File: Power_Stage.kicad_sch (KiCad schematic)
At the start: 95 parts, among them CN11 XH-2A, CN12 XH-2A, CN8 XH-2A, CN9 XH-2A, U16 LMR50410XDBVR, U17 LMR50410XDBVR, U3 BQ25792RQMR, U4 INA228AIDGSR, U5 TPS56A37RPAR, U6 IHLP3232DZER3R3M01, U9 SN74LVC1G32DBVR

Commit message: 1
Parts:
- removed C28: 100uF, EasyEDA:CAP-SMD_BD6.3-L6.6-W6.6-LS7.2-R-RD, symbol JLSC:RVT1E101M0607
- removed CN12: XH-2A, EasyEDA:CONN-TH_XH-2A, symbol JLSC:XH-2A
- removed R16: 10K, fb_2, symbol JLSC:0603WAF1002T5E
- removed TP4: 3.3V_AON Test Point, TestPoint:TestPoint_Pad_D1.5mm, symbol Connector:TestPoint
- removed TP5: V_BAT Test Point, TestPoint:TestPoint_Pad_D1.5mm, symbol Connector:TestPoint
- removed TP6: V_BUS Test Point, TestPoint:TestPoint_Pad_D1.5mm, symbol Connector:TestPoint
- added R45: 0603WAF1002T5E, EasyEDA:R0603, symbol JLSC:0603WAF1002T5E
- added R46: 10K, EasyEDA:R0603, symbol JLSC:0603WAF1002T5E
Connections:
- net 5VREG_EN: now also R46.1
- net GND: now also R45.2
- net GNDA: now also R46.2
- net at R23.2, R24.1, U3.16 (TS): now also R45.1

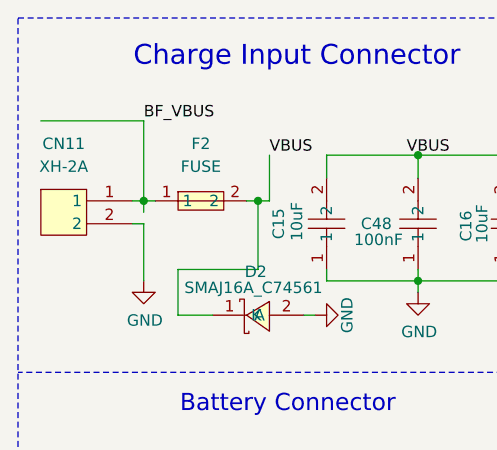
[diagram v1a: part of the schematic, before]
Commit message: micro hdmi eklendi
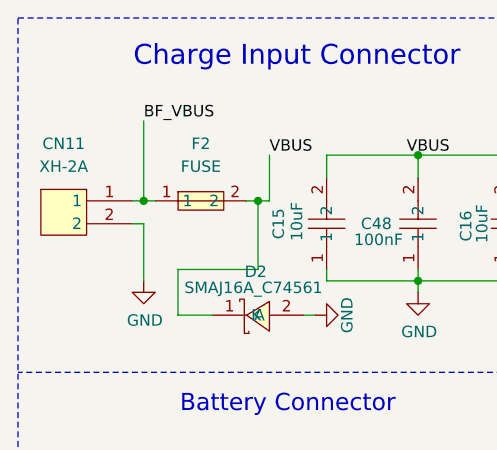
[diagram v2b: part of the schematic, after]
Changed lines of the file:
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@@
 	)
 	(junction
-		(at 35.56 40.64)
-		(diameter 0)
-		(color 0 0 0 0)
-	)
-	(junction
 		(at 82.55 228.6)
 		(diameter 0)
@@
 	)
 	(junction
+		(at 35.56 40.64)
+		(diameter 0)
+		(color 0 0 0 0)
+	)
+	(junction
 		(at 46.99 219.71)
 		(diameter 0)
@@
 	(wire
 		(pts
-			(xy 24.13 31.75) (xy 35.56 31.75)
-		)
-		(stroke
-			(width 0)
-			(type default)
-		)
-	)
-	(wire
-		(pts
 			(xy 287.02 233.68) (xy 287.02 227.33)
 		)
@@
 	(wire
 		(pts
+			(xy 35.56 40.64) (xy 36.83 40.64)
+		)
+		(stroke
+			(width 0)
+			(type default)
+		)
+	)
+	(wire
+		(pts
 			(xy 217.17 160.02) (xy 228.6 160.02)
 		)
@@
 	(wire
 		(pts
-			(xy 35.56 31.75) (xy 35.56 40.64)
-		)
-		(stroke
-			(width 0)
-			(type default)
-		)
-	)
-	(wire
-		(pts
 			(xy 57.15 241.3) (xy 55.88 241.3)
 		)
@@
 	(wire
 		(pts
-			(xy 35.56 40.64) (xy 36.83 40.64)
-		)
-		(stroke
-			(width 0)
-			(type default)
-		)
-	)
-	(wire
-		(pts
 			(xy 69.85 254) (xy 71.12 254)
 		)
@@
 	(wire
 		(pts
-			(xy 35.56 41.91) (xy 35.56 40.64)
-		)
-		(stroke
-			(width 0)
-			(type default)
-		)
-	)
-	(wire
-		(pts
 			(xy 243.84 57.15) (xy 252.73 57.15)
 		)
@@
 		)
 		(stroke
+			(width 0)
+			(type default)
+		)
+	)
+	(wire
+		(pts
+			(xy 35.56 31.75) (xy 35.56 40.64)
+		)
+		(stroke

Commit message: Hdmi
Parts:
- removed D1: SMBJ13A_C188307, EasyEDA:SMB_L4.6-W3.6-LS5.3-RD, symbol JLSC:SMBJ13A_C188307
- added D3: SMBJ14A_C353392, EasyEDA:SMB_L4.4-W3.6-LS5.3-RD, symbol JLSC:SMBJ14A_C353392
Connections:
- net GND: now also D3.2 (A)
- net V_BAT: now also D3.1 (C)
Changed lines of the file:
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@@
 	)
 	(symbol
+		(lib_id "JLSC:SMBJ14A_C353392")
+		(at 71.12 95.25 270)
+		(unit 1)
+		(body_style 1)
+		(exclude_from_sim no)
+		(in_bom yes)
+		(on_board yes)
+		(in_pos_files yes)
+		(dnp no)
+		(property "Reference" "D3"
+			(at 74.93 93.4699 90)
+			(show_name no)
+			(do_not_autoplace no)
+			(effects
+				(font
+					(size 1.27 1.27)
+				)
+				(justify left)
+			)
+		)
+		(property "Value" "SMBJ14A_C353392"
+			(at 50.038 95.504 90)
+			(show_name no)
+			(do_not_autoplace no)
+			(effects
+				(font
+					(size 1.27 1.27)
+				)
+				(justify left)
+			)
+		)
+		(property "Footprint" "EasyEDA:SMB_L4.4-W3.6-LS5.3-RD"
+			(at 63.5 95.25 0)
+			(hide yes)
+			(show_name no)
+			(do_not_autoplace no)
+			(effects
+				(font
+					(size 1.27 1.27)
+				)
+			)
+		)
+		(property "Datasheet" "https://lcsc.com/product-detail/Others_Shandong-Jingdao-Microelectronics-SMBJ14A_C353392.html"
+			(at 60.96 95.25 0)
+			(hide yes)
+			(show_name no)
+			(do_not_autoplace no)
+			(effects
+				(font
+					(size 1.27 1.27)
+				)
+			)
+		)
+		(property "Description" "SMBJ series 600W 14V Uni-directional SMD TVS Diode"
+			(at 71.12 95.25 0)
+			(hide yes)
+			(show_name no)
+			(do_not_autoplace no)
+			(effects
+				(font
+					(size 1.27 1.27)
+				)
+			)
+		)
+		(property "Manufacturer" "晶导微电子"
+			(at 58.42 95.25 0)
+			(hide yes)
+			(show_name no)
+			(do_not_autoplace no)
+			(effects
+				(font
+					(size 1.27 1.27)
+				)
+			)
+		)
+		(property "MPN" "SMBJ14A"
+			(at 55.88 95.25 0)
+			(hide yes)
+			(show_name no)
+			(do_not_autoplace no)
+			(effects
+				(font
+					(size 1.27 1.27)
+				)
+			)
+		)
+		(property "LCSC Part" "C353392"
+			(at 53.34 95.25 0)
+			(hide yes)
+			(show_name no)
+			(do_not_autoplace no)
+			(effects
+				(font
+					(size 1.27 1.27)
+				)
+			)
+		)
+		(pin "1"
+		)
+		(pin "2"
+		)
+		(instances
+			(project "Orbit Mini Mainboard"
+				(path "/3febad84-6a46-4f67-b4f6-fd06fdd71423/c9d5f001-0b8b-4865-8b52-75391c5f367e"
+					(reference "D3")
+					(unit 1)
+				)
+			)
+		)
+	)
+	(symbol
 		(lib_id "power:PWR_FLAG")
 		(at 189.23 223.52 90)
@@
 					(unit 1)
 				)
-			)
-		)
-	)
-	(symbol
-		(lib_id "JLSC:SMBJ13A_C188307")
-		(at 71.12 95.25 270)
-		(unit 1)
-		(body_style 1)
-		(exclude_from_sim no)
-		(in_bom yes)
-		(on_board yes)
-		(in_pos_files yes)
-		(dnp no)
-		(fields_autoplaced yes)
-		(property "Reference" "D1"
-			(at 77.47 94.995 0)
-			(show_name no)
-			(do_not_autoplace no)
-			(effects
-				(font
-					(size 1.27 1.27)
-				)
-			)
-		)
-		(property "Value" "SMBJ13A_C188307"
-			(at 74.93 94.995 0)
-			(show_name no)
-			(do_not_autoplace no)
-			(effects
-				(font
-					(size 1.27 1.27)
-				)
-			)
-		)
-		(property "Footprint" "EasyEDA:SMB_L4.6-W3.6-LS5.3-RD"
-			(at 63.5 95.25 0)
-			(hide yes)
-			(show_name no)
-			(do_not_autoplace no)
-			(effects
-				(font
-					(size 1.27 1.27)
-				)
-			)
-		)
-		(property "Datasheet" "https://lcsc.com/product-detail/TVS_SMBJ13A_C188307.html"
-			(at 60.96 95.25 0)
-			(hide yes)
-			(show_name no)
-			(do_not_autoplace no)
-			(effects
-				(font
-					(size 1.27 1.27)
-				)
-			)
-		)
-		(property "Description" ""
-			(at 71.12 95.25 0)
-			(hide yes)
-			(show_name no)
-			(do_not_autoplace no)
-			(effects
-				(font
-					(size 1.27 1.27)
-				)
-			)
-		)
-		(property "Manufacturer" "FMS(美丽微)"
-			(at 58.42 95.25 0)
-			(hide yes)
-			(show_name no)
-			(do_not_autoplace no)
-			(effects
-				(font
-					(size 1.27 1.27)
-				)
-			)
-		)
-		(property "MPN" "SMBJ13A"
-			(at 55.88 95.25 0)
-			(hide yes)
-			(show_name no)
-			(do_not_autoplace no)
-			(effects
-				(font
-					(size 1.27 1.27)
-				)
-			)
-		)
-		(property "LCSC Part" "C188307"
-			(at 53.34 95.25 0)
-			(hide yes)
-			(show_name no)
-			(do_not_autoplace no)
-			(effects
-				(font
-					(size 1.27 1.27)
-				)
-			)
-		)
-		(pin "2"
-		)
-		(pin "1"
-		)
-		(instances
-			(project "Orbit Mini Mainboard"
-				(path "/3febad84-6a46-4f67-b4f6-fd06fdd71423/c9d5f001-0b8b-4865-8b52-75391c5f367e"
-					(reference "D1")
-					(unit 1)
-				)
